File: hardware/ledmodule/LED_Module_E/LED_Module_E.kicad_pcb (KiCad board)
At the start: 4 copper layers, 33 x 81 mm, 87 parts, among them J1 USB4125-GF-A, J2 Conn_02x11_Odd_Even, Q1 Si3456DDV, Q11 Si3456DDV, Q12 Si3456DDV, Q2 Si3456DDV, Q3 Si3456DDV, Q4 Si3456DDV, Q5 Si3456DDV, Q6 Si3456DDV, Q7 Si3456DDV, Q8 Si3456DDV, U1 TMP1075DGK, U2 74HCT244, U3 24AA02UIDT-I/OT

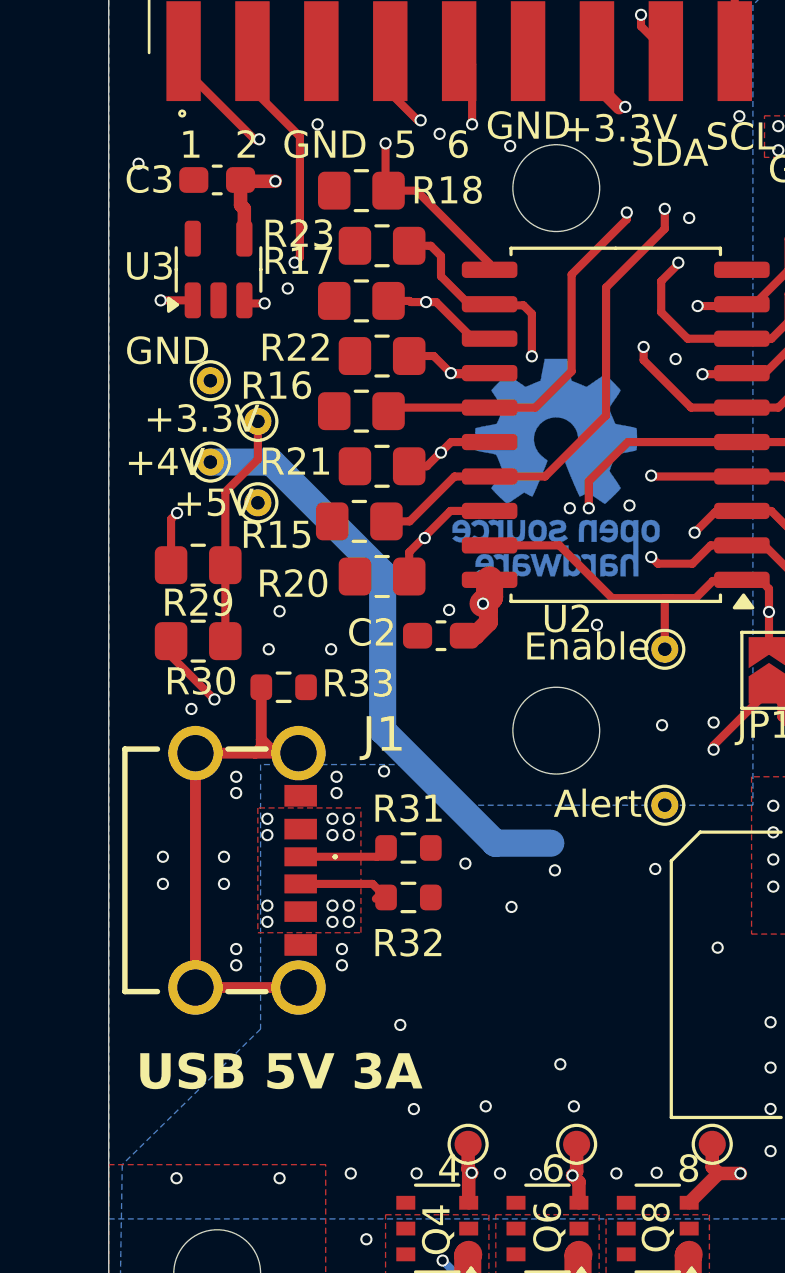
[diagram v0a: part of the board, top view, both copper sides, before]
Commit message: Fix / add meta data in title_block for all LED modules.
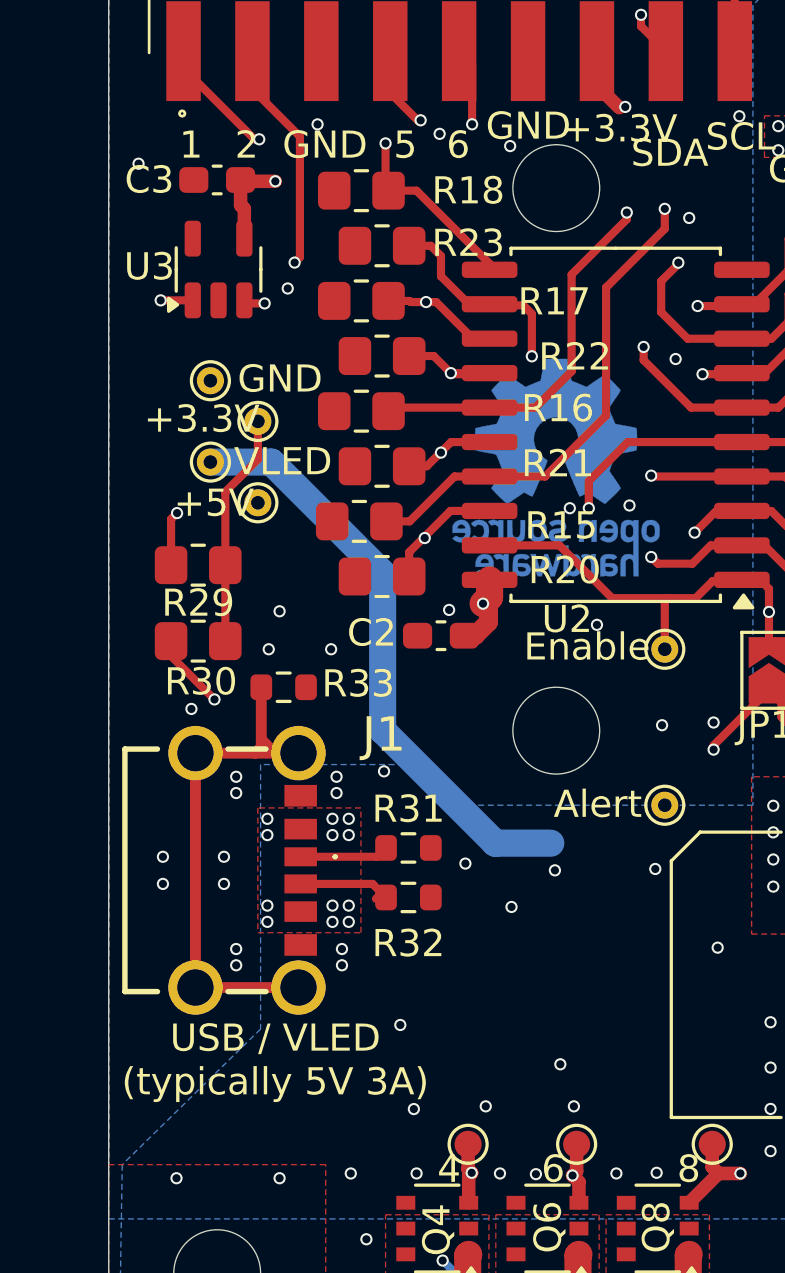
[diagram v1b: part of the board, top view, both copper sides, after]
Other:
- board text added: "LED Module E v1.1"
- board text added: "USB / VLED (typically 5V 3A)"
- board text removed: "+4V"
- board text removed: "LED Module E v1.0"
- board text removed: "USB 5V 3A"

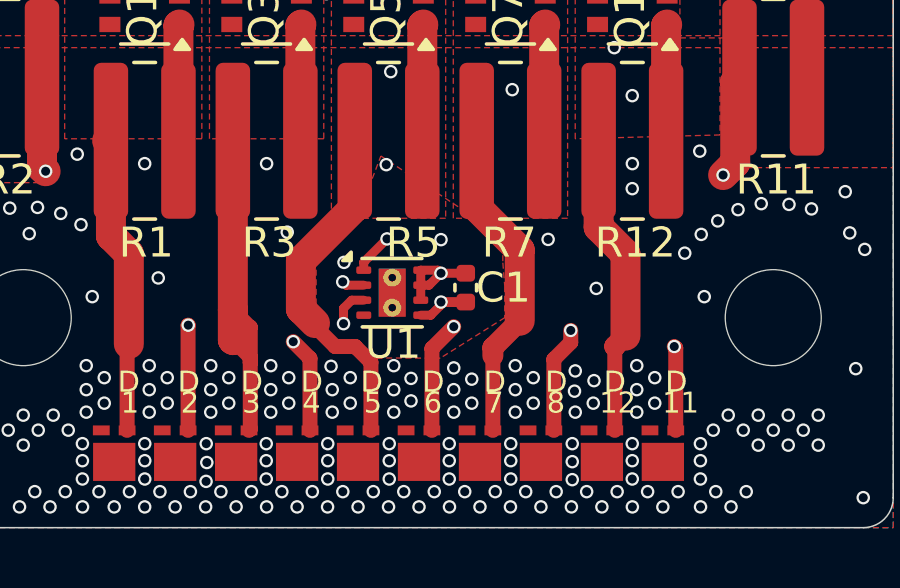
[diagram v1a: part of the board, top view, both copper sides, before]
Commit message: Probably minor changes (specific R values, etc.)
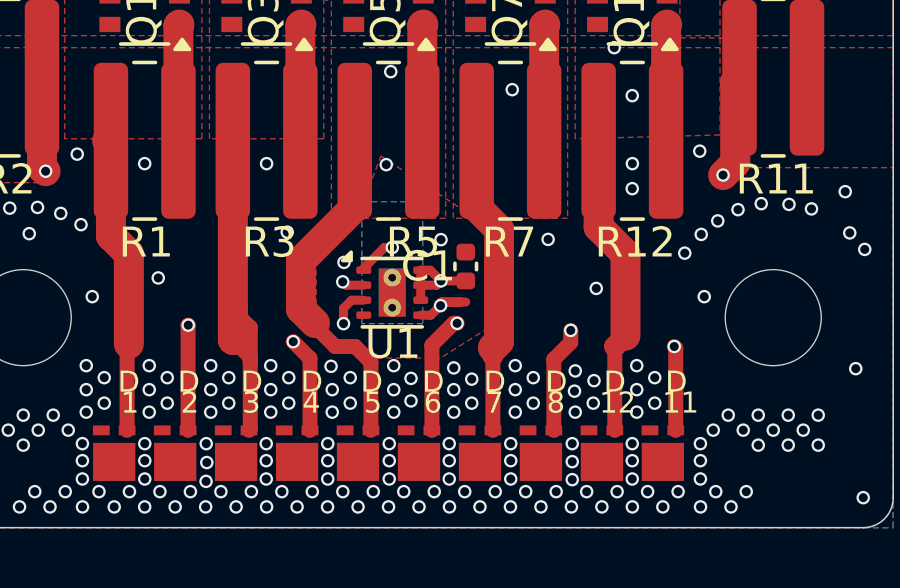
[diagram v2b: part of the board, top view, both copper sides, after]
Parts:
- R10, R13, R14, R15, R16, R17, R18, R19, R20, R21, R22, R23, R24, R25, R26, R27, R28, R29, R30, R9: value R_Small -> 2740R
- moved C1 0.70 mm to (140.8, 74.3), turned to -90 degrees
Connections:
- U1 pad 9: +4V -> GND
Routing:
- net +4V: track 23.2 -> 21.8 mm
- net Net-(D7-K): track 10.6 -> 10.0 mm

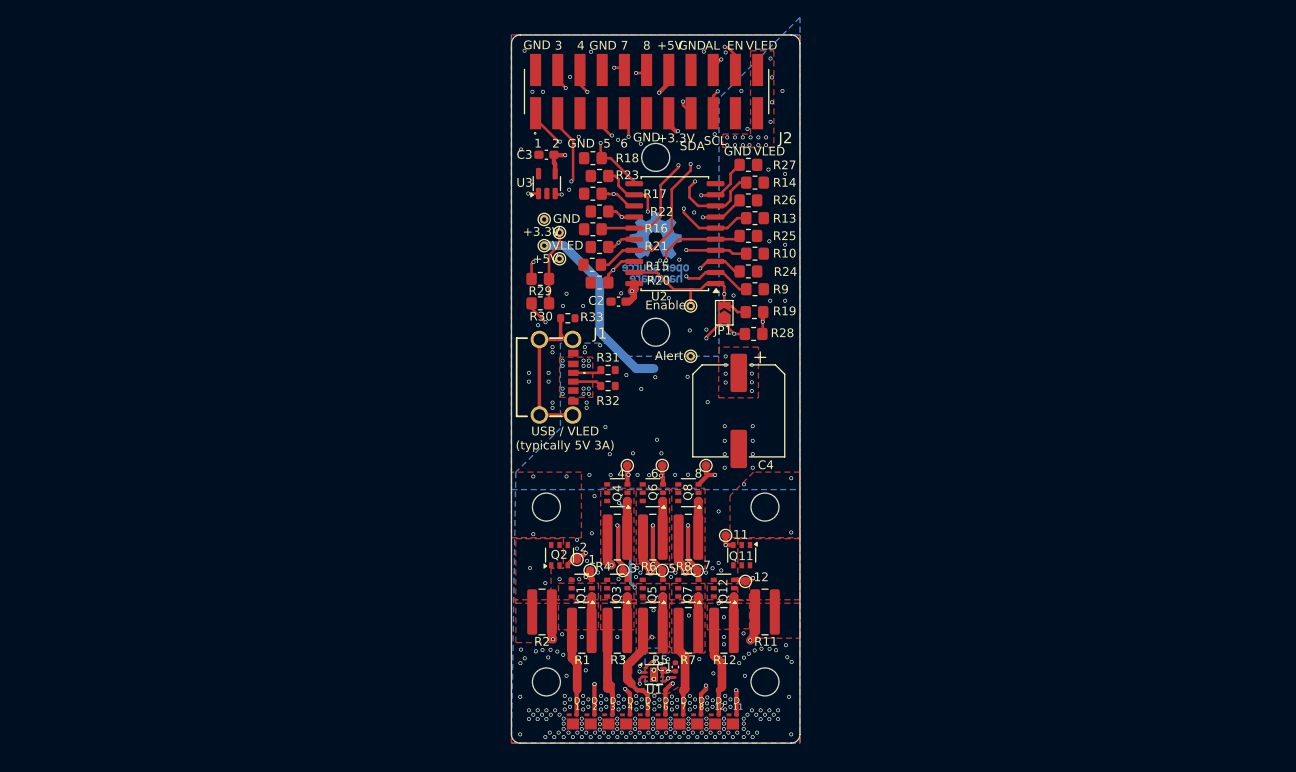
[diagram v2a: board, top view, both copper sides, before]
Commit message: Complete redesign of LED Module E for the ABL.
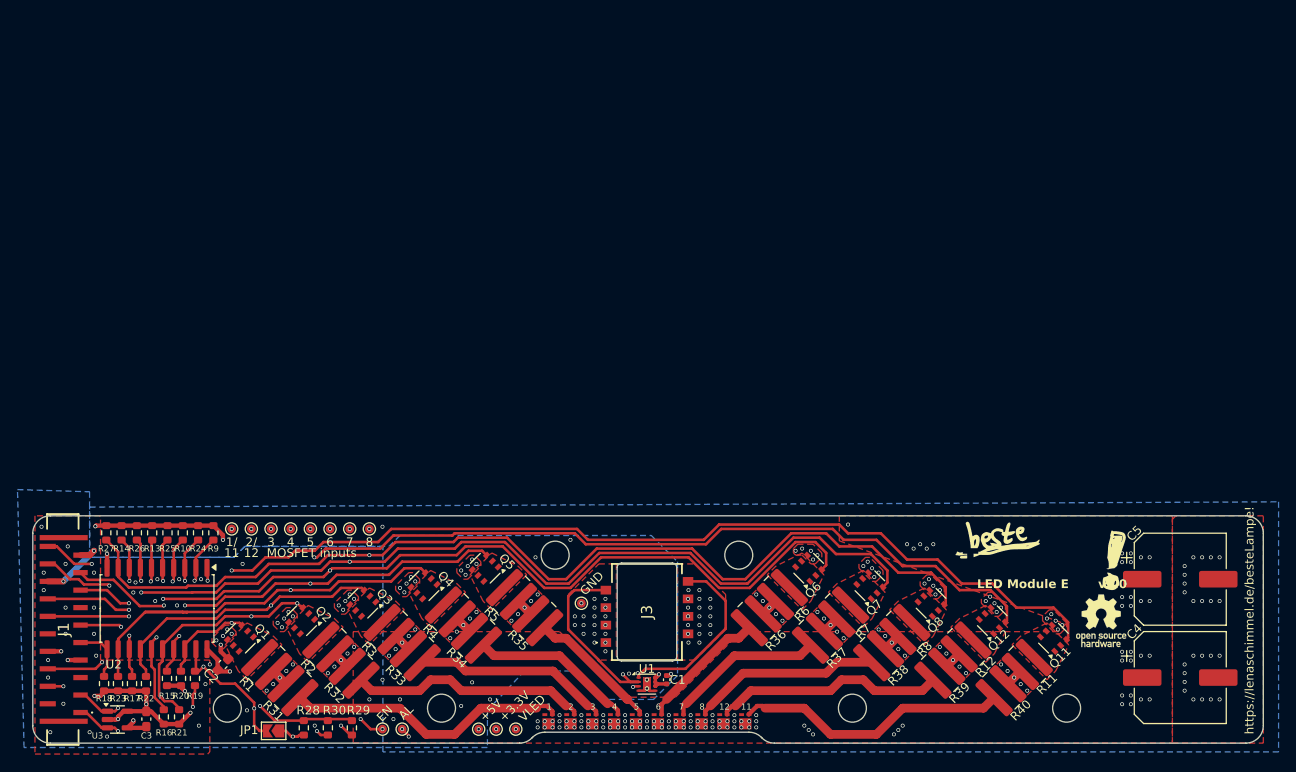
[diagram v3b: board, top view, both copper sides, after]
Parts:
- removed J2: Conn_02x11_Odd_Even, TSM-111-01-T-DV:TSM-111-YY-ZZZ-DV
- removed TP15, TP16: TestPoint, TestPoint:TestPoint_Pad_D1.0mm
- added C5: 680uF, Capacitor_SMD:CP_Elec_10x7.9, F.Cu at (198.5, 64.2)
- added J3: 009159008603906, 009159008603906:009159008603906, F.Cu at (137.5, 68.0)
- added R34: 220mR, Resistor_SMD:R_1020_2550Metric, F.Cu at (118.0, 71.0)
- added R35: 220mR, Resistor_SMD:R_1020_2550Metric, F.Cu at (125.0, 69.0)
- added R36: 220mR, Resistor_SMD:R_1020_2550Metric, F.Cu at (150.0, 69.0)
- added R37: 220mR, Resistor_SMD:R_1020_2550Metric, F.Cu at (157.0, 71.0)
- added R38: 220mR, Resistor_SMD:R_1020_2550Metric, F.Cu at (164.0, 73.0)
- added R39: 220mR, Resistor_SMD:R_1020_2550Metric, F.Cu at (171.0, 75.0)
- added R40: 220mR, Resistor_SMD:R_1020_2550Metric, F.Cu at (178.0, 77.0)
- G***: moved to F.Cu
- J1: value USB4125-GF-A -> SFW20S-2STE1LF; footprint USB4125-GF-A:USB4125GFA -> SFW20S-2STE1LF:SFW20S2STE1LF
- LOGO1: footprint Symbol:OSHW-Logo_7.5x8mm_Copper -> Symbol:OSHW-Logo_5.7x6mm_SilkScreen; moved to F.Cu
- R1, R11: value 200mR -> 220mR
- R10, R13, R14, R15, R16, R17, R18, R19, R20, R21, R22, R23, R24, R25, R26, R27, R28, R29, R30, R9: footprint Resistor_SMD:R_0805_2012Metric_Pad1.20x1.40mm_HandSolder -> Resistor_SMD:R_0603_1608Metric
- R12, R2, R3, R4, R5, R6, R7, R8: value 133mR -> 220mR
- R31, R32, R33: value 5100R -> 220mR; footprint Resistor_SMD:R_0603_1608Metric -> Resistor_SMD:R_1020_2550Metric
- TP1, TP2, TP3, TP4, TP5, TP6: footprint TestPoint:TestPoint_THTPad_D1.0mm_Drill0.5mm -> TestPoint:TestPoint_Pad_D1.0mm
- moved R27 84.6 mm to (75.7, 58.9), turned to 90 degrees
- moved R14 82.8 mm to (77.4, 58.9), turned to 90 degrees
- moved R18 82.1 mm to (75.4, 76.2), turned to -90 degrees
- moved R23 80.0 mm to (77.0, 76.2), turned to -90 degrees
- moved R26 79.6 mm to (79.2, 58.9), turned to 90 degrees
- moved C3 79.1 mm to (80.2, 80.2), turned to -90 degrees
- moved U3 78.5 mm to (76.9, 80.3), turned to 0 degrees
- moved R13 77.8 mm to (80.9, 58.9), turned to 90 degrees
- moved R17 76.9 mm to (78.6, 76.2), turned to -90 degrees
- moved R19 76.5 mm to (85.8, 75.6), turned to -90 degrees
- moved R22 74.9 mm to (80.2, 76.2), turned to -90 degrees
- moved R25 74.6 mm to (82.7, 58.9), turned to 90 degrees
- moved R16 74.3 mm to (82.2, 80.0), turned to -90 degrees
- moved U2 73.1 mm to (81.5, 67.6), turned to -90 degrees
- moved R10 72.8 mm to (84.4, 58.9), turned to 90 degrees
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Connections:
- R1 pad 1: Net-(D1-K) -> Net-(R1-Pad1)
- R11 pad 1: Net-(D11-K) -> Net-(R11-Pad1)
- R12 pad 1: Net-(D12-K) -> Net-(R12-Pad1)
- R2 pad 1: Net-(D2-K) -> Net-(R2-Pad1)
- R3 pad 1: Net-(D3-K) -> Net-(R3-Pad1)
- R31 pad 1: Net-(J1-CC1) -> Net-(D1-K)
- R31 pad 2: GND -> Net-(R1-Pad1)
- R32 pad 1: Net-(J1-CC2) -> Net-(D2-K)
- R32 pad 2: GND -> Net-(R2-Pad1)
- R33 pad 1: Net-(J1-PadMH1) -> Net-(D3-K)
- R33 pad 2: GND -> Net-(R3-Pad1)
- R4 pad 1: Net-(D4-K) -> Net-(R34-Pad2)
- R5 pad 1: Net-(D5-K) -> Net-(R35-Pad2)
- R6 pad 1: Net-(D6-K) -> Net-(R36-Pad2)
- R7 pad 1: Net-(D7-K) -> Net-(R37-Pad2)
- R8 pad 1: Net-(D8-K) -> Net-(R38-Pad2)
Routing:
- net Net-(Q8-G): track 46.1 -> 116.9 mm
- net Net-(Q1-G): track 66.0 -> 127.8 mm
- net Net-(Q6-G): track 38.8 -> 99.7 mm, vias 2 -> 4
- net Net-(Q12-G): track 70.1 -> 130.4 mm, vias 3 -> 4
- net Net-(Q7-G): track 49.5 -> 108.4 mm, vias 2 -> 4
- net GND: track 2.91 -> 44.2 mm, vias 107 -> 141
- net Net-(D1-K): track 10.1 -> 32.6 mm
- net Net-(J1-PadMH1): track 20.3 -> 0.00 mm
- net /i7: track 30.6 -> 10.9 mm
- net /i4: track 35.4 -> 16.0 mm
- net Net-(D11-K): track 13.2 -> 31.6 mm, vias 2 -> 0
- net /i8: track 23.2 -> 6.61 mm, vias 2 -> 0
- net /i1: track 39.0 -> 22.6 mm
- net /ALERT: track 94.6 -> 78.2 mm
- net Net-(D12-K): track 10.2 -> 26.5 mm
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- added copper zone on F.Cu, net Net-(R1-Pad1)
- added copper zone on F.Cu, net Net-(R11-Pad1)
- added copper zone on In2.Cu, net Net-(R11-Pad1)
- added copper zone on F.Cu, net Net-(R12-Pad1)
- added copper zone on In2.Cu, net Net-(R12-Pad1)
- added copper zone on F.Cu, net Net-(R2-Pad1)
- added copper zone on F.Cu, net Net-(R3-Pad1)
- added copper zone on F.Cu, net Net-(R34-Pad2)
- added copper zone on F.Cu, net Net-(R35-Pad2)
- added copper zone on F.Cu, net Net-(R36-Pad2)
- added copper zone on In2.Cu, net Net-(R36-Pad2)
- added copper zone on F.Cu, net Net-(R37-Pad2)
- added copper zone on In2.Cu, net Net-(R37-Pad2)
- added copper zone on F.Cu, net Net-(R38-Pad2)
- added copper zone on In2.Cu, net Net-(R38-Pad2)
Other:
- board size 33 x 81 mm -> 140.8 x 26 mm
- board text added: "1/"
- board text added: "2/"
- board text added: "LED Module E v2.0"
- board text added: "MOSFET inputs"
- board text removed: "Alert"
- board text removed: "D"
- board text removed: "Enable"
- board text removed: "LED Module E v1.1"
- board text removed: "SCL"
- board text removed: "SDA"
- board text removed: "USB / VLED (typically 5V 3A)"

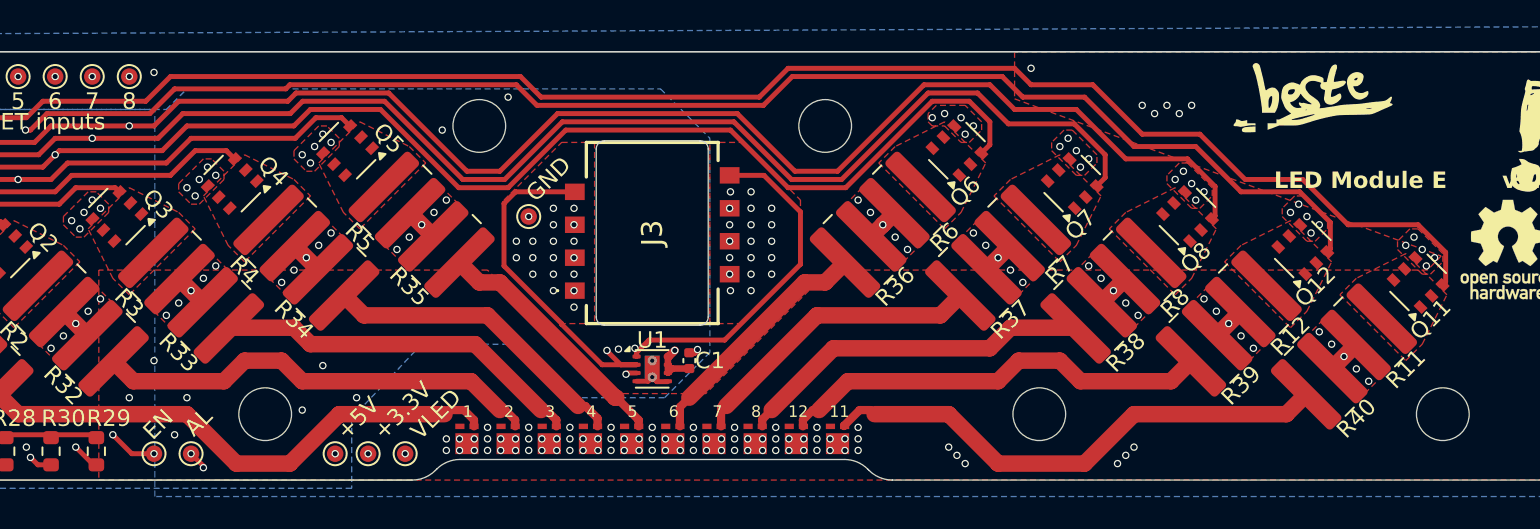
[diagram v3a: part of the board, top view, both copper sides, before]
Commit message: Mirror the connector, optimize VLED between connector and LEDs.
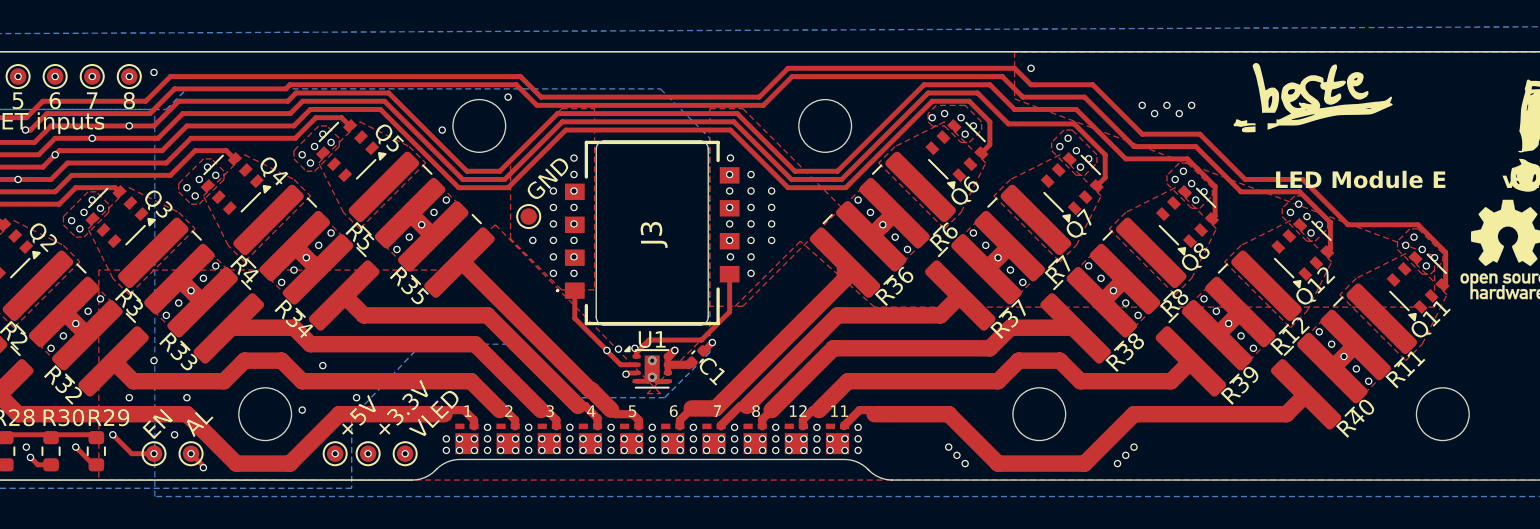
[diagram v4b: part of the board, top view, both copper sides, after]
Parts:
- moved C1 0.56 mm to (140.2, 75.5), turned to -135 degrees
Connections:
- J3 pad 1: GND -> /SCL
- J3 pad 2: +4V -> /SDA
- J3 pad 7: /SCL -> GND
- J3 pad 8: /SDA -> +4V
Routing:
- net /SCL: track 93.2 -> 78.7 mm
- net /SDA: track 94.3 -> 82.7 mm
- net GND: track 44.2 -> 44.4 mm, vias 141 -> 137
- net +4V: vias 129 -> 128
